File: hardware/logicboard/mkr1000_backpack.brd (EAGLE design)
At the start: 25 x 61.5 mm, 2 parts, among them J4 DNP, J5 DNP

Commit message: Analog pins.
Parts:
- added ANALOG: (no value), SparkFun-Connectors:2X4
- added RN1: (no value), resistor-net:RN-5
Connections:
- new net A0: ANALOG.1, J4.2, RN1.5
- new net A1: ANALOG.3, J4.3, RN1.4
- new net A2: ANALOG.5, J4.4, RN1.3
- new net A3: ANALOG.7, J4.5, RN1.2
- new net GND: J5.11, RN1.1
- new net VCC: ANALOG.2, ANALOG.4, ANALOG.6, ANALOG.8, J5.12
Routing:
- net A3: track 0.00 -> 42.2 mm
- net A0: track 0.00 -> 29.2 mm, vias 0 -> 1
- net VCC: track 0.00 -> 27.3 mm
- net A1: track 0.00 -> 24.2 mm, vias 0 -> 1
- net A2: track 0.00 -> 21.7 mm, vias 0 -> 1
- net GND: track 0.00 -> 19.6 mm
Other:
- board text added: "MKR1000 BACKPACK 1.0.0"
- board text added: "Pineapple"

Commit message: First try.
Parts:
- added RN2: 10k, resistor-net:RN-5
- ANALOG: device SparkFun-Connectors:2X4 -> con-ml:ML10L
- RN1: value (none) -> 10k
- moved ANALOG 7.00 mm to (12.5, 43.0)
- moved RN1 5.00 mm to (12.5, 37.0)
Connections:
- removed net A0: ANALOG.1, J4.2, RN1.5
- new net A4: ANALOG.8, J4.6, RN1.2
- new net A5: ANALOG.10, J4.7, RN2.5
- net A1: now also ANALOG.2, RN1.5; no longer ANALOG.3, RN1.4
- net A2: now also ANALOG.4, RN1.4; no longer ANALOG.5, RN1.3
- net A3: now also ANALOG.6, RN1.3; no longer ANALOG.7, RN1.2
- net GND: now also RN2.1
- net VCC: now also ANALOG.1, ANALOG.3, ANALOG.5, ANALOG.7, ANALOG.9; no longer ANALOG.2, ANALOG.4, ANALOG.6, ANALOG.8
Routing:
- net A4: track 0.00 -> 44.0 mm
- net A5: track 0.00 -> 33.7 mm
- net A0: track 29.2 -> 0.00 mm, vias 1 -> 0
- net A3: track 42.2 -> 22.4 mm, vias 0 -> 1
- net A2: track 21.7 -> 37.2 mm, vias 1 -> 0
- net VCC: track 27.3 -> 20.6 mm
- net GND: track 19.6 -> 20.7 mm
- net A1: track 24.2 -> 25.0 mm, vias 1 -> 0
- added copper zone on layer 1, net GND
- added copper zone on layer 16, net GND

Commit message: Second try. Looks good.
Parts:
- J4, J5: device MK1_Zero:STRIP-14-MODULI-A11 -> SparkFun-Connectors:1X14
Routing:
- net A4: track 44.0 -> 27.0 mm
- net A2: track 37.2 -> 26.8 mm
- net A1: track 25.0 -> 30.4 mm
- net A5: track 33.7 -> 31.5 mm
- net A3: track 22.4 -> 22.3 mm, vias 1 -> 0

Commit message: Backside mounting.
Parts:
- flipped ANALOG to the bottom
- flipped RN1 to the bottom
- flipped RN2 to the bottom
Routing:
- net GND: track 20.2 -> 9.75 mm
- net A5: track 31.5 -> 23.1 mm
- net A2: track 26.8 -> 19.3 mm
- net A1: track 30.4 -> 24.8 mm
- net A4: track 27.0 -> 32.4 mm

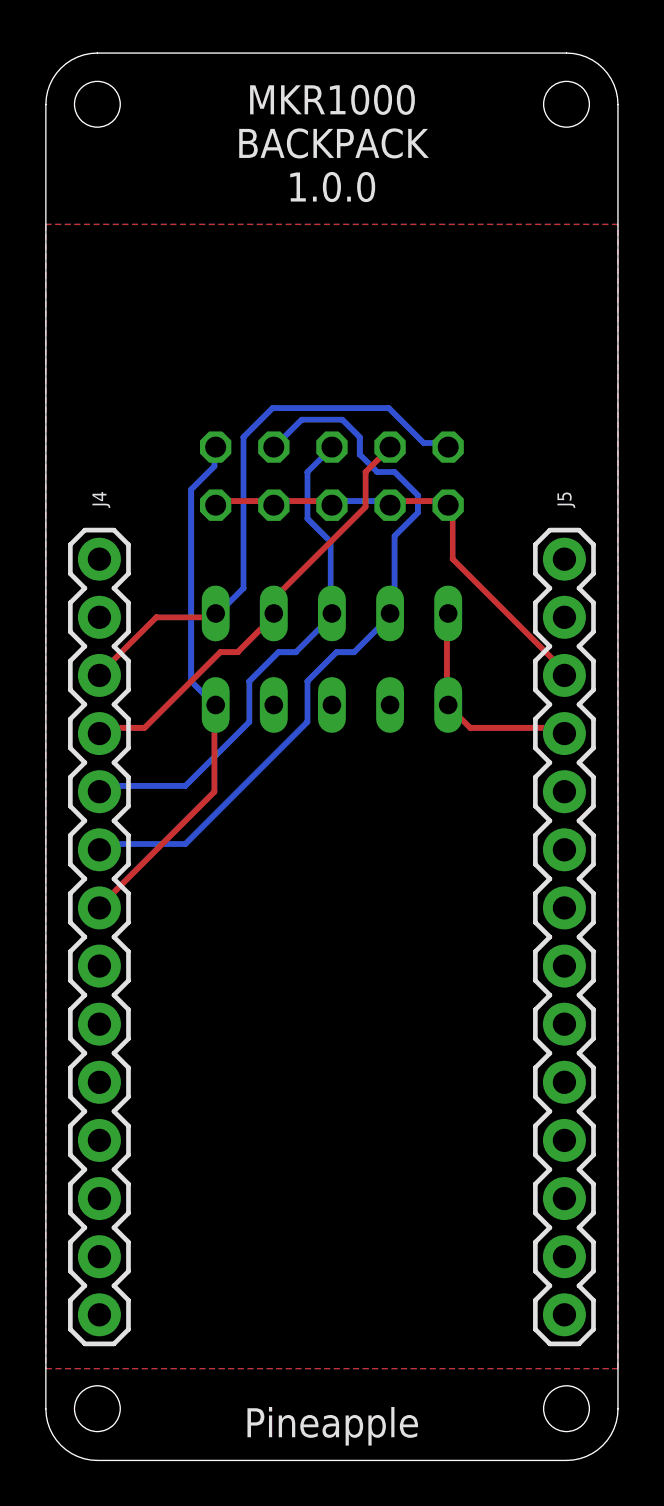
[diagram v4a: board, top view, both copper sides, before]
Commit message: Added encoder switch for selecting IP address.
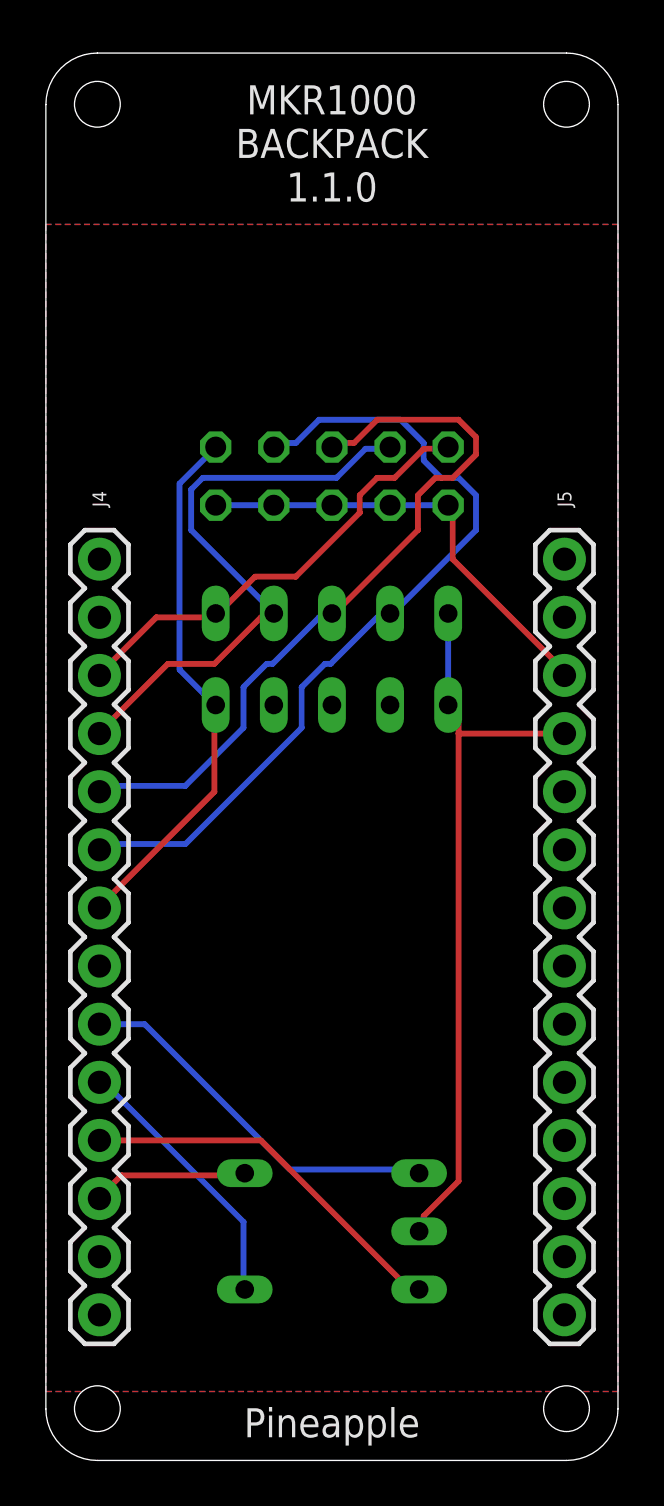
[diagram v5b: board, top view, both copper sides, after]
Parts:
- added IPADDRESS: (no value), switch-dil:A1353HEX
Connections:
- new net D0: IPADDRESS.1, J4.9
- new net D1: IPADDRESS.2, J4.10
- new net D2: IPADDRESS.4, J4.11
- new net D3: IPADDRESS.8, J4.12
- net GND: now also IPADDRESS.C
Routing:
- net GND: track 9.75 -> 32.5 mm
- net D0: track 0.00 -> 16.7 mm
- net D2: track 0.00 -> 16.7 mm
- net D1: track 0.00 -> 11.8 mm
- net A3: track 22.6 -> 32.4 mm
- net A2: track 19.3 -> 26.2 mm
- net D3: track 0.00 -> 6.84 mm
- net A1: track 24.8 -> 19.9 mm
- net A4: track 32.4 -> 36.0 mm
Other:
- board text added: "MKR1000 BACKPACK 1.1.0"
- board text removed: "MKR1000 BACKPACK 1.0.0"

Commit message: Moved 10p MIL connector up by 1mm.
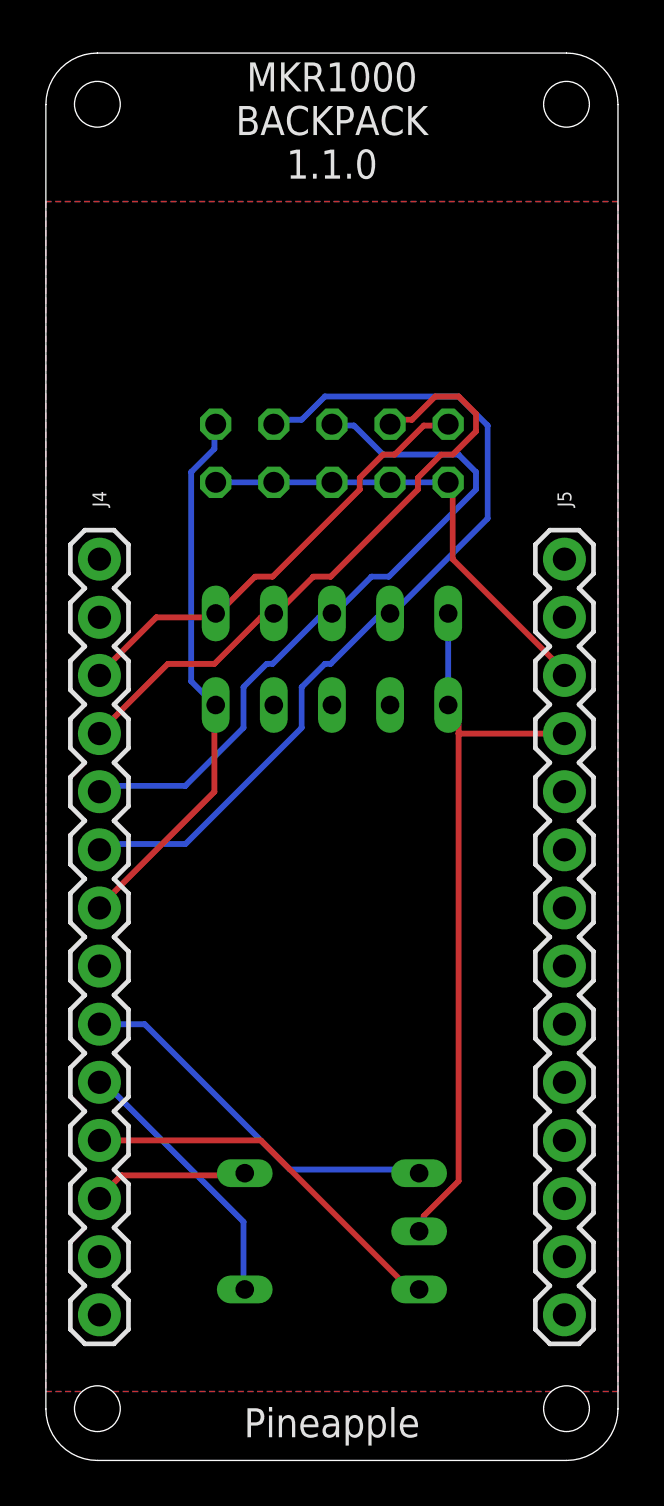
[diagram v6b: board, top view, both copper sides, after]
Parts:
- moved ANALOG 1.00 mm to (12.5, 44.0)
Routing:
- net A4: track 36.0 -> 38.5 mm
- net A3: track 32.4 -> 30.9 mm
- net A2: track 26.2 -> 27.6 mm
- net VCC: track 20.2 -> 21.2 mm
- net A5: track 23.5 -> 24.1 mm

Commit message: Capacitor.
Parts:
- added C1: 0.1u, resistor:C025-025X050
- ANALOG: device con-ml:ML10L -> con-ml:ML14L
- moved RN1 5.00 mm to (12.5, 32.0)
- moved RN2 5.00 mm to (12.5, 28.0)
- moved ANALOG 2.00 mm to (12.5, 46.0)
- moved IPADDRESS 1.00 mm to (12.5, 11.0)
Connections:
- new net A0: ANALOG.2, J4.2, RN1.5
- new net A6: ANALOG.14, J4.8, RN2.3
- net A1: now also ANALOG.4, RN1.4; no longer ANALOG.2, RN1.5
- net A2: now also ANALOG.6, RN1.3; no longer ANALOG.4, RN1.4
- net A3: now also ANALOG.8, RN1.2; no longer ANALOG.6, RN1.3
- net A4: now also ANALOG.10, RN2.5; no longer ANALOG.8, RN1.2
- net A5: now also ANALOG.12, RN2.4; no longer ANALOG.10, RN2.5
- net GND: now also C1.2
- net VCC: now also ANALOG.11, ANALOG.13, C1.1
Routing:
- net A0: track 0.00 -> 37.8 mm
- net A6: track 0.00 -> 36.1 mm
- net A5: track 24.1 -> 50.1 mm
- net A1: track 20.1 -> 37.1 mm
- net VCC: track 21.2 -> 32.3 mm
- net A2: track 27.6 -> 35.2 mm
- net A4: track 38.5 -> 32.0 mm
- net GND: track 32.5 -> 36.9 mm
- net A3: track 30.9 -> 32.3 mm
- net D1: track 11.8 -> 10.8 mm

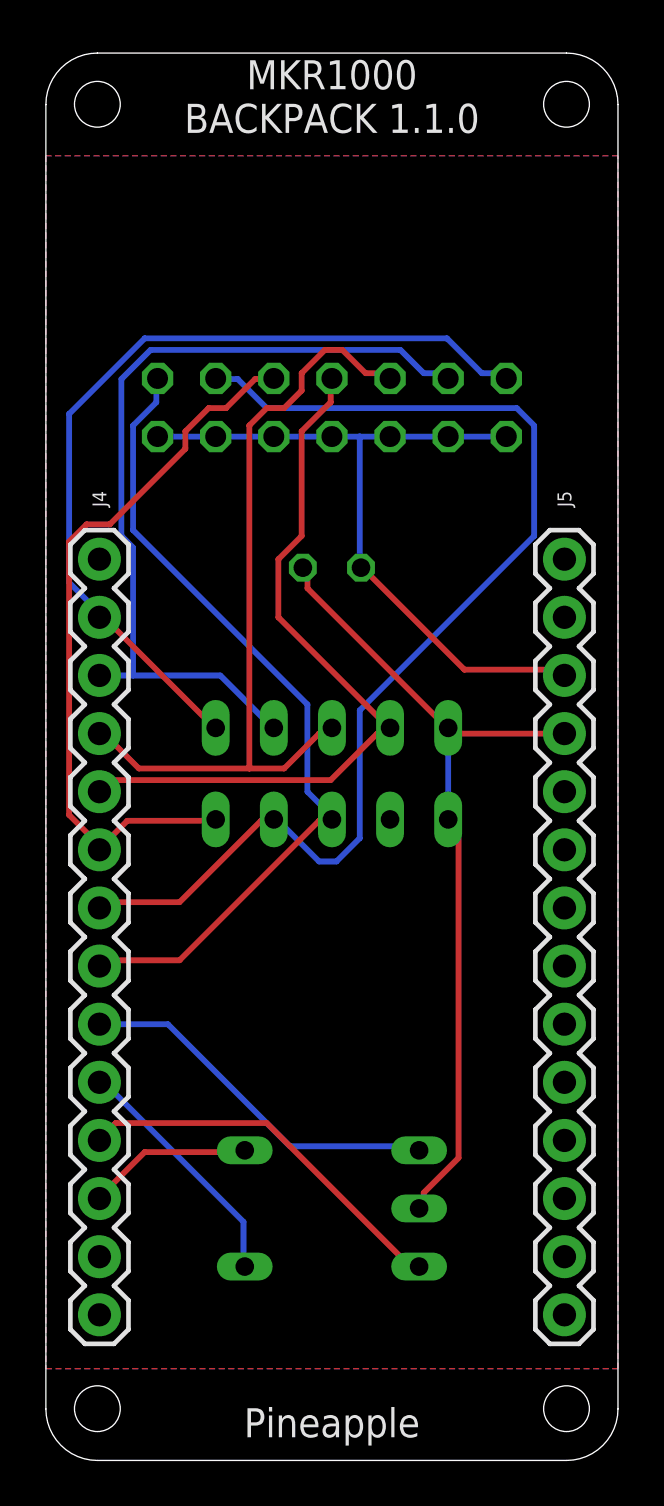
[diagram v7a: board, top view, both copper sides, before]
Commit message: LED ports and I2C port.
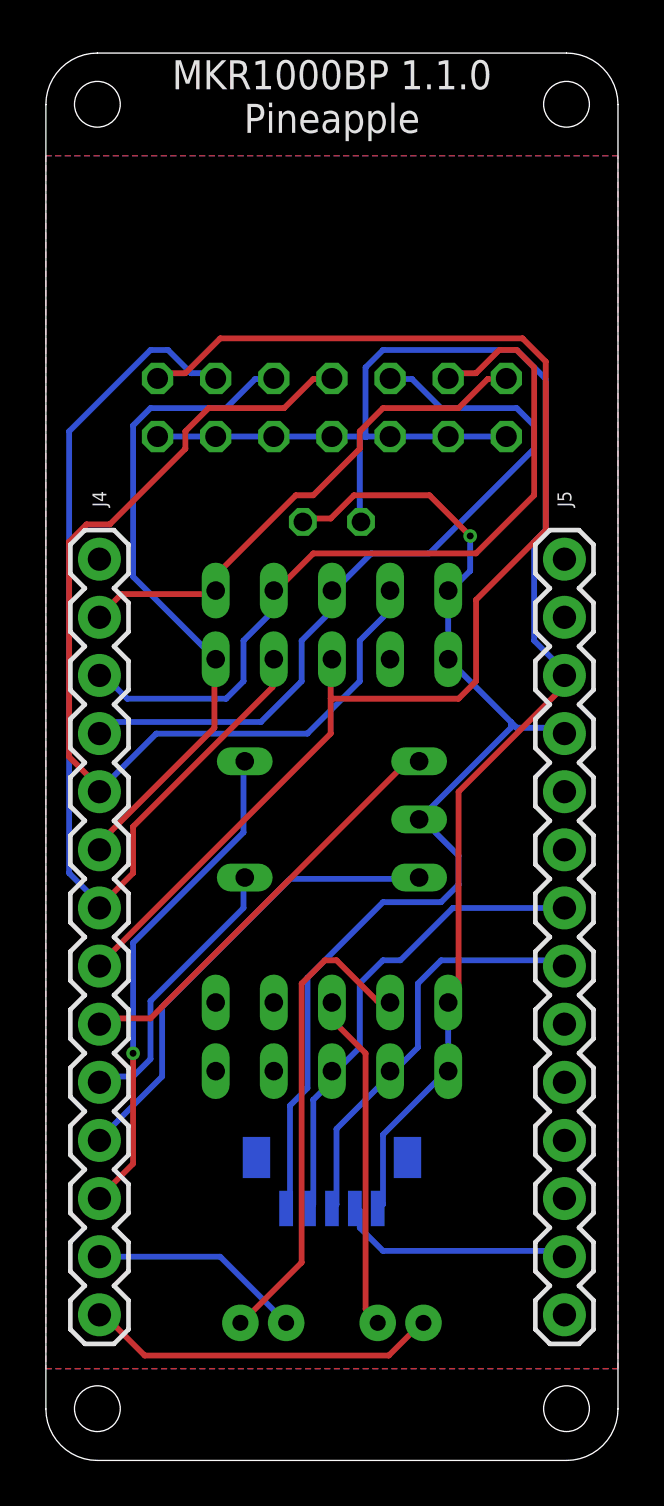
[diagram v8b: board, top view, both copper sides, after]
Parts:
- added J1, J2: (no value), SparkFun-Connectors:JST-2-PTH-NS
- added J3: 3.3V, SparkFun-Connectors:1X05_1MM
- added RN3: 680, resistor-net:RN-5
- added RN4: 6.8k, resistor-net:RN-5
- moved IPADDRESS 17.0 mm to (12.5, 28.0)
- moved RN2 7.00 mm to (12.5, 35.0)
- moved RN1 6.00 mm to (12.5, 38.0)
- moved C1 2.00 mm to (12.5, 41.0)
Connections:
- new net D7: J3.2, J5.2
- new net N$1: J1.1, RN3.2
- new net N$2: J2.1, RN3.3
- new net N$3: J1.2, J4.13
- new net N$4: J2.2, J4.14
- new net SCL: J3.3, J5.7, RN4.2
- new net SDA: J3.4, J5.8, RN4.3
- net GND: now also J3.5
- net VCC: now also J3.1, RN3.1, RN4.1
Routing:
- net VCC: track 32.3 -> 71.7 mm
- net A6: track 36.1 -> 57.6 mm
- net SDA: track 0.00 -> 21.3 mm
- net N$1: track 0.00 -> 21.0 mm
- net SCL: track 0.00 -> 18.5 mm
- net N$4: track 0.00 -> 15.5 mm
- net N$2: track 0.00 -> 14.8 mm
- net A0: track 37.8 -> 23.0 mm
- net D3: track 7.25 -> 21.7 mm, vias 0 -> 1
- net GND: track 36.9 -> 49.2 mm, vias 0 -> 1
- net A3: track 32.3 -> 44.2 mm
- net D7: track 0.00 -> 10.6 mm
- net N$3: track 0.00 -> 9.36 mm
- net A5: track 50.1 -> 43.8 mm
- net D2: track 17.0 -> 20.5 mm
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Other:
- board text added: "MKR1000BP 1.1.0 Pineapple"
- board text removed: "MKR1000 BACKPACK 1.1.0"
- board text removed: "Pineapple"
